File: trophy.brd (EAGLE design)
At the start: 75.9 x 26.7 mm, 20 parts, among them J1 AVR_SPI_PROG_3X2PTH, U1 ATTINY85SOIC8

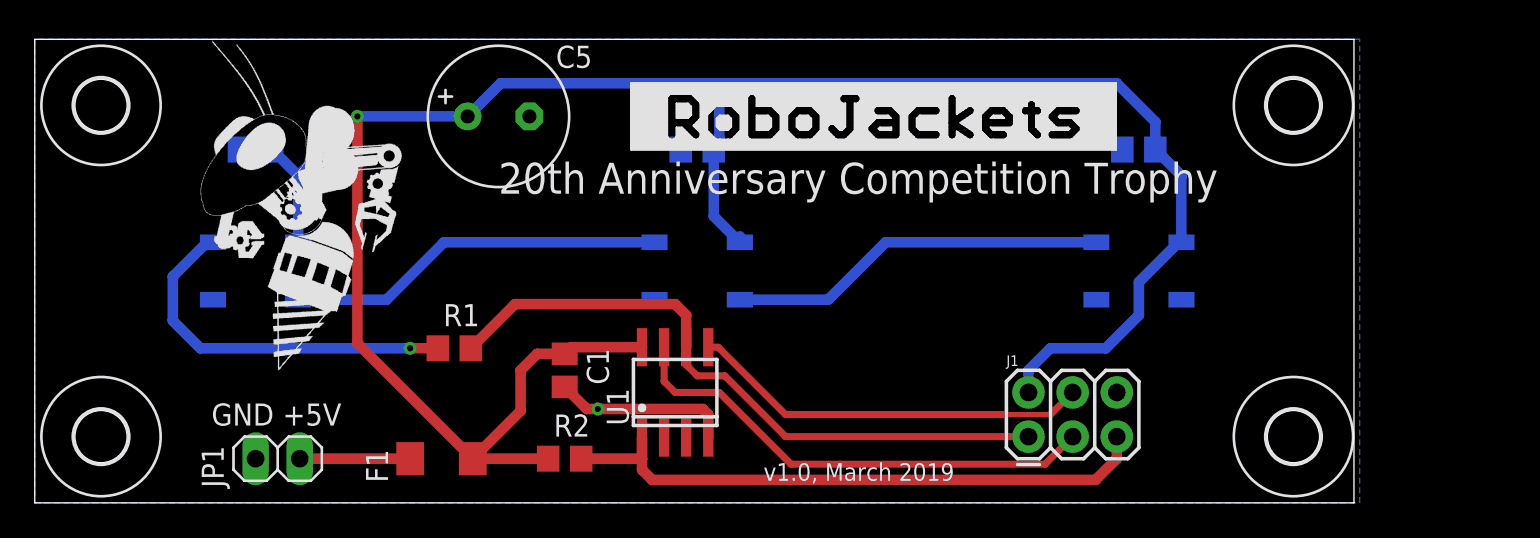
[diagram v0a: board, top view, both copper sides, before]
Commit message: Move caps to give more clearance for acrylic holder
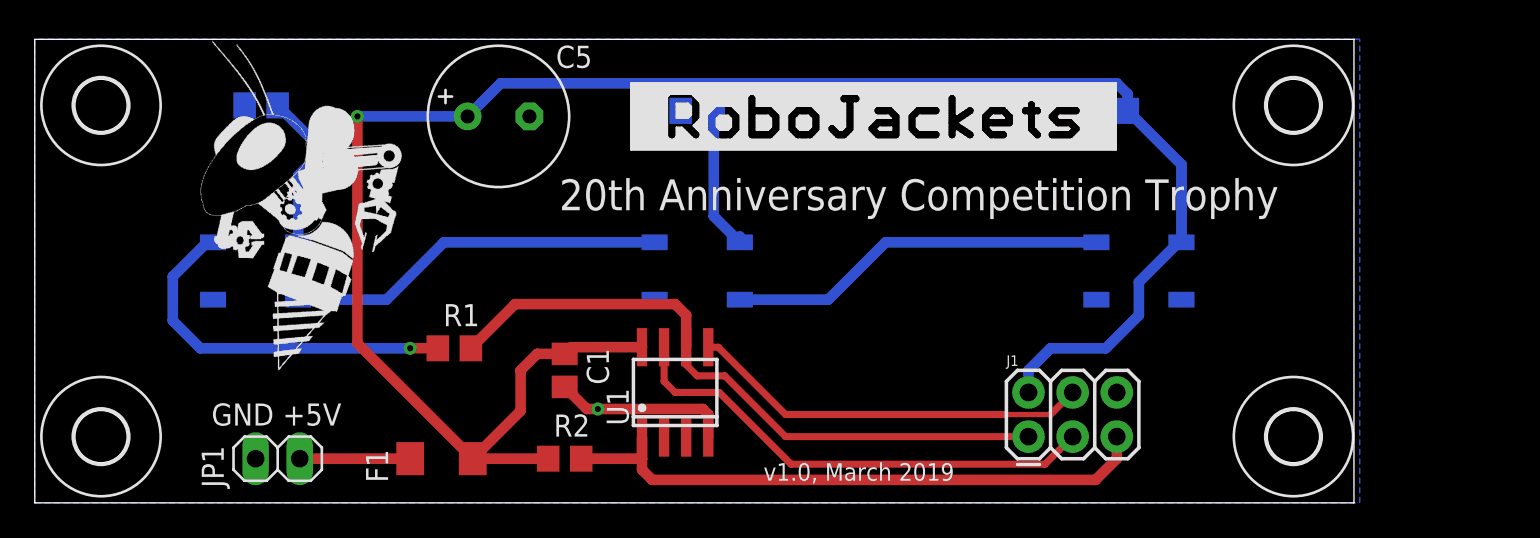
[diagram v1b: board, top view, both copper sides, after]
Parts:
- moved C2 2.73 mm to (61.9, 22.5)
- moved C4 2.56 mm to (13.0, 22.9)
- moved C3 2.22 mm to (38.1, 22.5)
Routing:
- net VCC: track 130.9 -> 132.5 mm
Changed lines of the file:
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@@
 <wire x1="0" y1="26.66" x2="0" y2="0" width="0" layer="20"/>
 <text x="10.16" y="4.445" size="1.27" layer="21">GND +5V</text>
-<text x="26.67" y="17.78" size="1.778" layer="21">20th Anniversary Competition Trophy</text>
+<text x="30.1625" y="16.8275" size="1.778" layer="21">20th Anniversary Competition Trophy</text>
 <text x="41.91" y="1.27" size="1.016" layer="21">v1.0, March 2019</text>
 </plain>
@@
 <attribute name="NAME" x="31.75" y="8.89" size="1.27" layer="25" font="vector" ratio="7" rot="R270"/>
 </element>
-<element name="C2" library="resistor" library_urn="urn:adsk.eagle:library:348" package="C0805" package3d_urn="urn:adsk.eagle:package:23617/2" value="0.1uF" x="63.5" y="20.32" smashed="yes" rot="MR0">
-<attribute name="NAME" x="64.77" y="21.59" size="1.27" layer="26" font="vector" ratio="7" rot="MR0"/>
-</element>
-<element name="C3" library="resistor" library_urn="urn:adsk.eagle:library:348" package="C0805" package3d_urn="urn:adsk.eagle:package:23617/2" value="0.1uF" x="38.1" y="20.32" smashed="yes" rot="MR0">
-<attribute name="NAME" x="39.37" y="21.59" size="1.27" layer="26" ratio="7" rot="MR0"/>
-</element>
-<element name="C4" library="resistor" library_urn="urn:adsk.eagle:library:348" package="C0805" package3d_urn="urn:adsk.eagle:package:23617/2" value="0.1uF" x="12.7" y="20.32" smashed="yes" rot="MR0">
-<attribute name="NAME" x="13.97" y="21.59" size="1.27" layer="26" font="vector" ratio="7" rot="MR0"/>
+<element name="C2" library="resistor" library_urn="urn:adsk.eagle:library:348" package="C0805" package3d_urn="urn:adsk.eagle:package:23617/2" value="0.1uF" x="61.9125" y="22.5425" smashed="yes" rot="MR0">
+<attribute name="NAME" x="63.1825" y="23.8125" size="1.27" layer="26" font="vector" ratio="7" rot="MR0"/>
+</element>
+<element name="C3" library="resistor" library_urn="urn:adsk.eagle:library:348" package="C0805" package3d_urn="urn:adsk.eagle:package:23617/2" value="0.1uF" x="38.1" y="22.5425" smashed="yes" rot="MR0">
+<attribute name="NAME" x="39.37" y="23.8125" size="1.27" layer="26" ratio="7" rot="MR0"/>
+</element>
+<element name="C4" library="resistor" library_urn="urn:adsk.eagle:library:348" package="C0805" package3d_urn="urn:adsk.eagle:package:23617/2" value="0.1uF" x="13.0175" y="22.86" smashed="yes" rot="MR0">
+<attribute name="NAME" x="14.2875" y="24.13" size="1.27" layer="26" font="vector" ratio="7" rot="MR0"/>
 </element>
 <element name="C5" library="JoshCustom" package="CAP-3,5-8" value="1000uF" x="26.67" y="22.225" smashed="yes">
@@
 <contactref element="F1" pad="1"/>
 <contactref element="C5" pad="POSITIVE"/>
-<wire x1="13.65" y1="20.32" x2="15.15" y2="18.82" width="0.6096" layer="16"/>
+<wire x1="13.9675" y1="22.86" x2="16.57875" y2="20.24875" width="0.6096" layer="16"/>
 <wire x1="15.15" y1="18.82" x2="15.15" y2="14.985" width="0.6096" layer="16"/>
 <wire x1="25.19" y1="2.54" x2="29.53" y2="2.54" width="0.6096" layer="1"/>
@@
 <wire x1="40.55" y1="15.33" x2="40.55" y2="14.985" width="0.6096" layer="16"/>
 <wire x1="24.892" y1="22.225" x2="18.555" y2="22.225" width="0.6096" layer="16"/>
-<wire x1="18.555" y1="22.225" x2="15.15" y2="18.82" width="0.6096" layer="16"/>
+<wire x1="18.555" y1="22.225" x2="16.57875" y2="20.24875" width="0.6096" layer="16"/>
+<wire x1="16.57875" y1="20.24875" x2="15.15" y2="18.82" width="0.6096" layer="16"/>
 <wire x1="25.19" y1="2.54" x2="18.555" y2="9.175" width="0.6096" layer="1"/>
 <wire x1="18.555" y1="9.175" x2="18.555" y2="22.225" width="0.6096" layer="1"/>
@@
 <wire x1="26.797" y1="24.13" x2="39.37" y2="24.13" width="0.6096" layer="16"/>
 <wire x1="39.37" y1="24.13" x2="62.23" y2="24.13" width="0.6096" layer="16"/>
-<wire x1="62.23" y1="24.13" x2="64.45" y2="21.91" width="0.6096" layer="16"/>
-<wire x1="64.45" y1="21.91" x2="64.45" y2="20.32" width="0.6096" layer="16"/>
-<wire x1="64.45" y1="20.32" x2="65.95" y2="18.82" width="0.6096" layer="16"/>
-<wire x1="65.95" y1="18.82" x2="65.95" y2="14.985" width="0.6096" layer="16"/>
-<wire x1="39.37" y1="24.13" x2="39.37" y2="20.64" width="0.6096" layer="16"/>
-<wire x1="39.37" y1="20.64" x2="39.05" y2="20.32" width="0.6096" layer="16"/>
-<wire x1="39.05" y1="20.32" x2="39.05" y2="16.485" width="0.6096" layer="16"/>
+<wire x1="62.23" y1="24.13" x2="62.8625" y2="23.4975" width="0.6096" layer="16"/>
+<wire x1="62.8625" y1="23.4975" x2="62.8625" y2="22.5425" width="0.6096" layer="16"/>
+<wire x1="62.8625" y1="22.5425" x2="65.95" y2="19.455" width="0.6096" layer="16"/>
+<wire x1="65.95" y1="19.455" x2="65.95" y2="14.985" width="0.6096" layer="16"/>
+<wire x1="39.37" y1="24.13" x2="39.37" y2="22.8625" width="0.6096" layer="16"/>
+<wire x1="39.37" y1="22.8625" x2="39.05" y2="22.5425" width="0.6096" layer="16"/>
+<wire x1="39.05" y1="22.5425" x2="39.05" y2="16.485" width="0.6096" layer="16"/>
 <wire x1="39.05" y1="16.485" x2="40.55" y2="14.985" width="0.6096" layer="16"/>
 <wire x1="57.15" y1="6.35" x2="57.15" y2="7.62" width="0.6096" layer="16"/>
